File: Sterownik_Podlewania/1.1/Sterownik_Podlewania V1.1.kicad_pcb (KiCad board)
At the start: 2 copper layers, 175 x 115 mm, 76 parts, among them J1 Barrel_Jack_MountingPin, J10 Screw_Terminal_01x02, J11 Screw_Terminal_01x02, J12 Screw_Terminal_01x02, J13 Screw_Terminal_01x02, J14 Screw_Terminal_01x02, J15 Screw_Terminal_01x02, J3 RJ45, J4 Conn_01x04_Socket, J5 RJ45, J8 RJ45, J9 Screw_Terminal_01x02, SW1 SW_Nidec_CAS-120A1, SW2 SW_Nidec_CAS-120A1, SW3 SW_Push_Dual_x2, SW4 SW_Push_Dual_x2, SW5 SW_Push_Dual_x2, SW6 SW_Push_Dual_x2, U1 ESP32-DEVKITC, U10 HHG1D-1, U11 757, U2 HHG1D-1, U3 L7805, U4 LD1117S33TR_SOT223, U5 757, U7 HHG1D-1, U8 HHG1D-1, U9 HHG1D-1

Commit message: Pociągnięcie prawie wszystkich ścieżek, dodanie rezystorów do I2C 5V
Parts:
- added R12: 4k7, Resistor_SMD:R_1206_3216Metric, B.Cu at (110.0, 80.0)
- added R14: 4k7, Resistor_SMD:R_1206_3216Metric, B.Cu at (106.5, 80.0)
- R21: value 130 -> 1300
- moved R10 56.6 mm to (185.0, 110.5)
- moved U5 22.3 mm to (131.7, 110.1), turned to 90 degrees
- moved R26 20.2 mm to (92.5, 132.5), turned to 0 degrees
- moved C3 20.2 mm to (92.5, 147.5)
- moved SW3 20.0 mm to (112.5, 140.6)
- moved R27 20.0 mm to (112.7, 132.5)
- moved SW4 20.0 mm to (92.5, 140.7)
- moved C4 19.9 mm to (112.5, 147.5)
- moved U11 19.4 mm to (154.3, 109.9), turned to 90 degrees
- moved J14 15.0 mm to (220.0, 70.0)
- moved J15 15.0 mm to (220.0, 55.0)
- moved R1 5.59 mm to (185.0, 86.5), turned to 90 degrees
- moved R2 2.50 mm to (185.0, 91.5)
- moved R3 2.50 mm to (211.5, 45.0)
- moved R5 2.50 mm to (211.5, 60.0)
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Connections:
- U1 pad 12: /DS_WYJŚCIE -> unconnected-(U1-IO14-Pad12)
- U1 pad 9: unconnected-(U1-IO25-Pad9) -> /DS_WYJŚCIE
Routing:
- net +5V: track 0.00 -> 342.0 mm
- net VP: track 0.00 -> 245.7 mm
- net +3.3V: track 0.00 -> 237.8 mm, vias 0 -> 1
- net SDA: track 0.00 -> 181.4 mm
- net SCL: track 0.00 -> 178.2 mm
- net Net-(J5-Pad7): track 0.00 -> 139.8 mm
- net /Pompa_230_5V: track 0.00 -> 138.9 mm, vias 0 -> 1
- net /SW1: track 0.00 -> 133.8 mm
- net /SEN0193_WYJŚCIE: track 0.00 -> 133.1 mm
- net /SW2: track 0.00 -> 112.9 mm
- net /Sekcja 5_5V: track 0.00 -> 105.1 mm, vias 0 -> 2
- net /DS_WYJŚCIE: track 0.00 -> 96.0 mm
- net /SW3: track 0.00 -> 95.0 mm
- net GND_VP: track 0.00 -> 91.9 mm
- net SDA_5V: track 0.00 -> 88.8 mm
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- added copper zone on B.Cu, net +3.3V
- added copper zone on B.Cu, net GND
- added copper zone on F.Cu, net GND

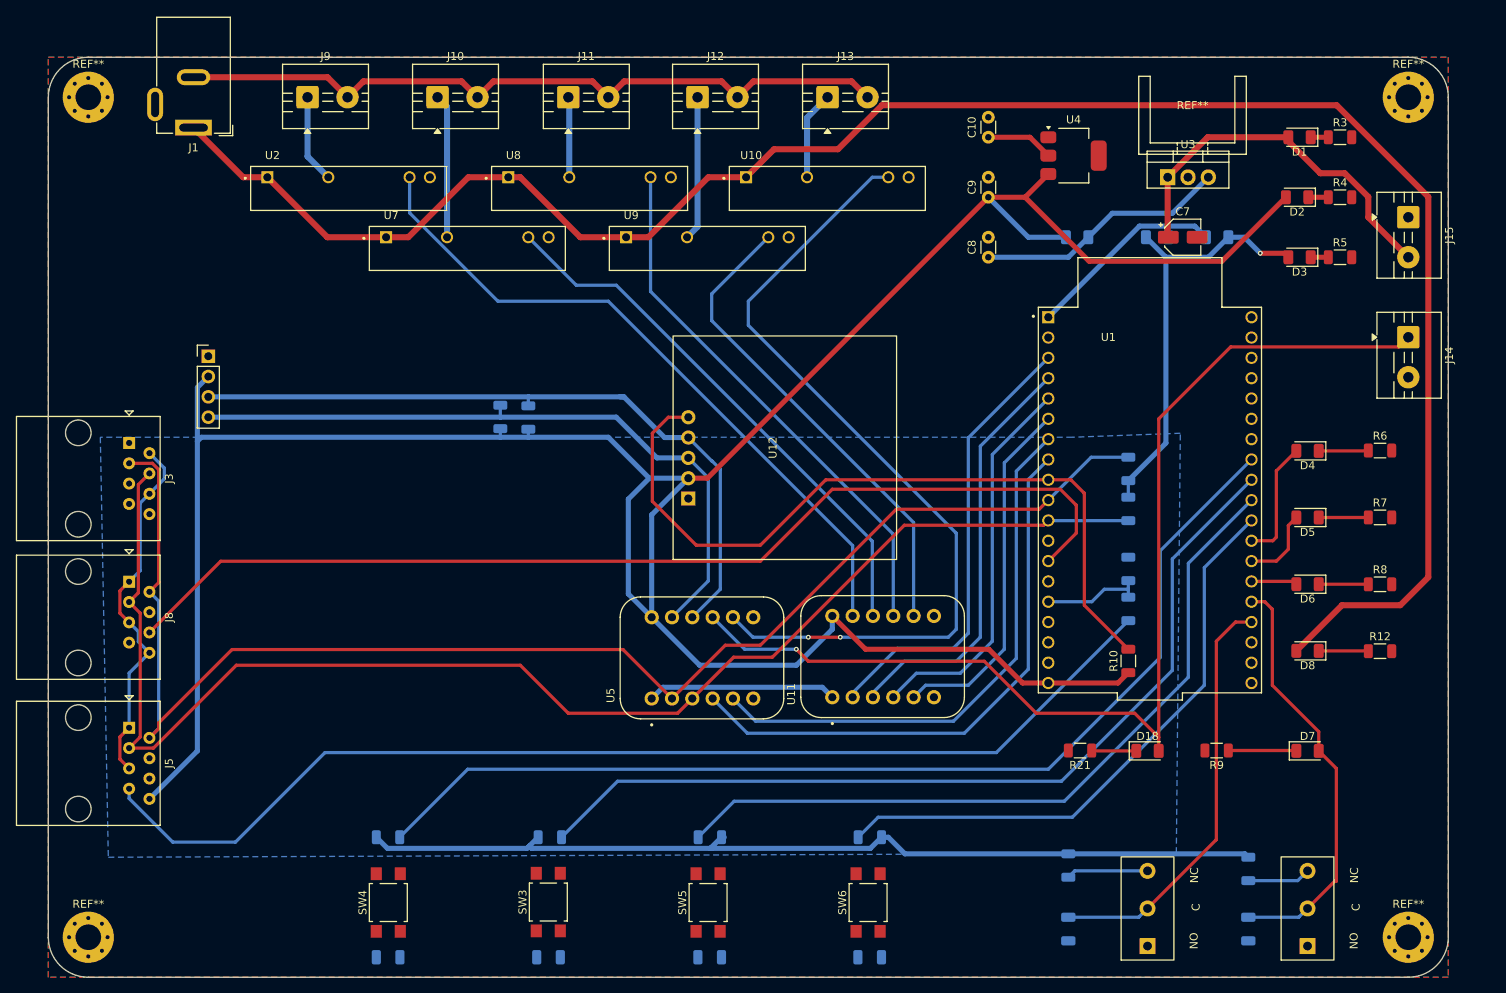
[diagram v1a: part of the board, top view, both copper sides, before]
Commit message: Poprawiono błędy połączeń SDA,SCL, dodno drugą magistralę I2C, pociągnięcie nowych ścieżek
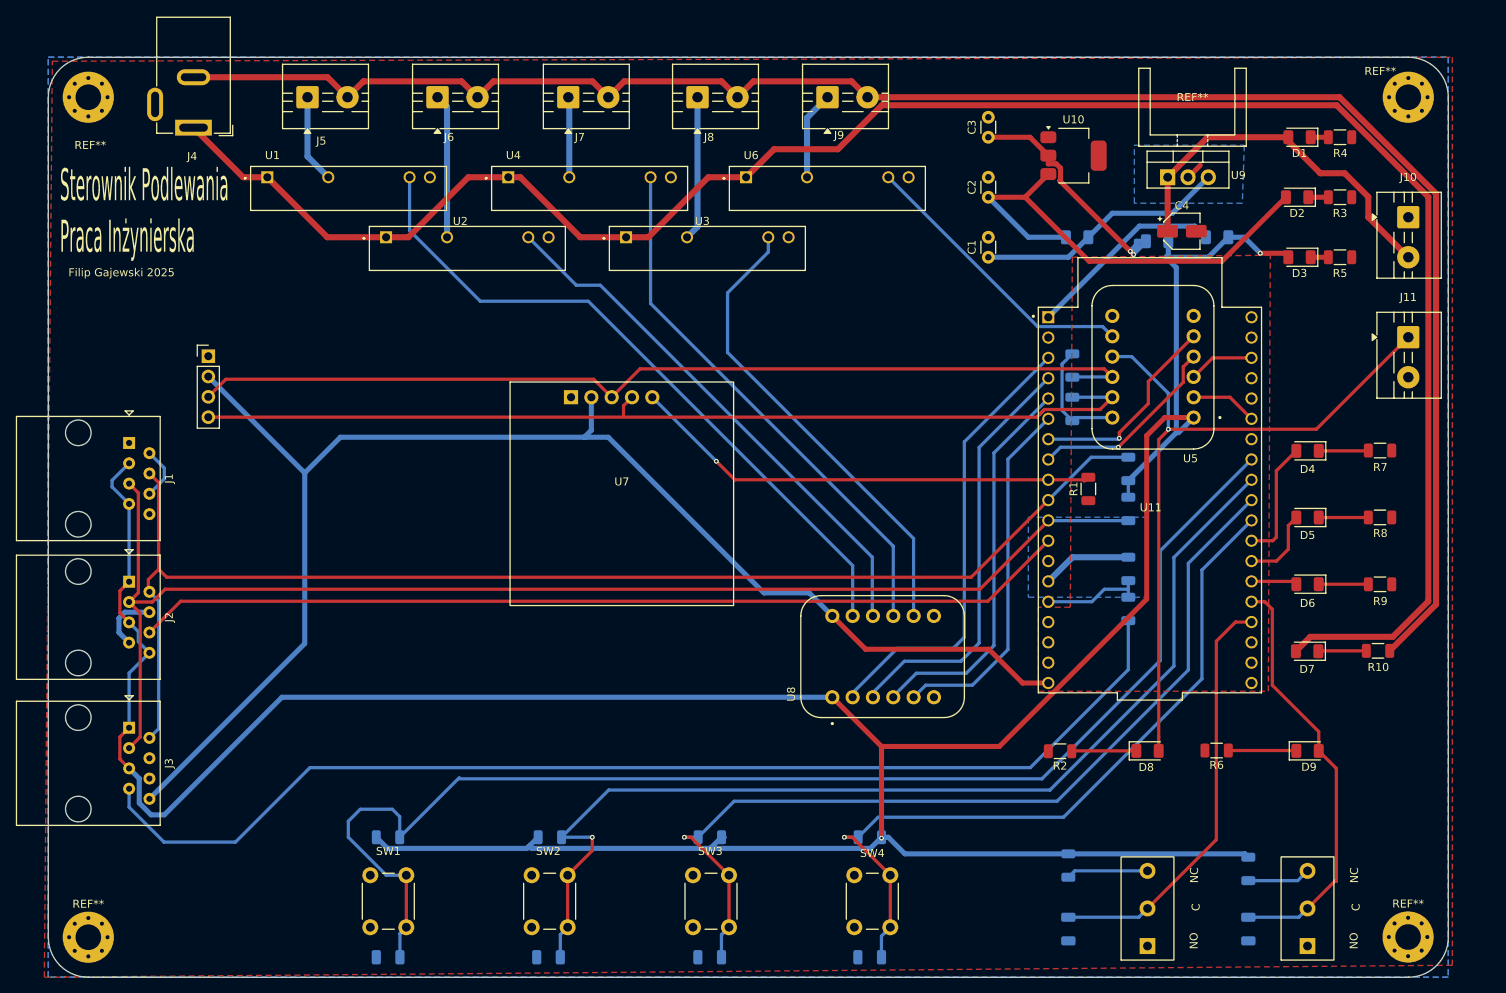
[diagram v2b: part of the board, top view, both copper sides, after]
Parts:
- removed the D8 at (207.4, 109.2)
- removed the R12 at (216.5, 109.2)
- removed the R21 at (179.0, 121.7)
- removed U12: ~, RTC:RTC DS1307 + 32kb EEPROM 24C32 I2C
- added D7: LED, LED_SMD:LED_1206_3216Metric, F.Cu at (207.3, 109.2)
- added R10: 2k2, Resistor_SMD:R_1206_3216Metric, F.Cu at (216.2, 109.2)
- added R2: 1300, Resistor_SMD:R_1206_3216Metric, F.Cu at (176.5, 121.8)
- added U7: ~, RTC:RTC DS1307 + 32kb EEPROM 24C32 I2C, F.Cu at (121.7, 89.6)
- SW1: renamed from SW4; footprint Button_Switch_SMD:SW_SPST_TL3305A -> Button_Switch_THT:SW_PUSH_6mm
- SW2: renamed from SW3; footprint Button_Switch_SMD:SW_SPST_TL3305A -> Button_Switch_THT:SW_PUSH_6mm
- SW3: renamed from SW5; footprint Button_Switch_SMD:SW_SPST_TL3305A -> Button_Switch_THT:SW_PUSH_6mm
- SW4: renamed from SW6; footprint Button_Switch_SMD:SW_SPST_TL3305A -> Button_Switch_THT:SW_PUSH_6mm
- moved R20 71.5 mm to (178.0, 79.0)
- moved R19 68.3 mm to (178.0, 73.5), turned to -90 degrees
- moved U5 67.1 mm to (188.1, 73.8), turned to 180 degrees
- moved R1 22.1 mm to (180.0, 89.0)
- moved SW1 3.82 mm to (90.2, 143.8)
- moved SW2 3.78 mm to (110.4, 143.8)
- moved SW3 3.62 mm to (130.6, 143.8)
- moved SW4 3.53 mm to (150.8, 143.8)
- moved REF** 1.01 mm to (193.0, 46.0)
- moved C4 0.76 mm to (191.7, 56.8)
- moved D11 0.50 mm to (188.6, 58.0), turned to 180 degrees
- renumbered C8 to C1, C3 to C10, C9 to C2, C10 to C3, C7 to C4, C1 to C5, C2 to C6, C6 to C7, C5 to C8, C4 to C9, D21 to D10, D20 to D11, D19 to D12, D18 to D8, D7 to D9, J3 to J1, J15 to J10, J14 to J11, J4 to J12, J8 to J2, J5 to J3, J1 to J4, J9 to J5, J10 to J6, J11 to J7, J12 to J8, J13 to J9, R10 to R1, R22 to R11, R1 to R12, R11 to R13, R13 to R14, R2 to R15, R23 to R16, R31 to R17, R28 to R18, R12 to R19, R14 to R20, R27 to R21, R26 to R22, R4 to R3, R3 to R4, R9 to R6, R6 to R7, R7 to R8, R8 to R9, SW2 to SW5, SW1 to SW6, U2 to U1, U4 to U10, U1 to U11, U7 to U2, U9 to U3, U8 to U4, U10 to U6, U11 to U8, U3 to U9
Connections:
- net SCL_5V renamed SCL_2_5V
- net SDA_5V renamed SDA_2_5V
- J1 pad 1: GND -> unconnected-(J1-Pad1)
- J1 pad 2: +3.3V -> GND
- J1 pad 3: SDA -> +3.3V
- J1 pad 4: SCL -> SDA_1
- J1 pad 5: GND -> SCL_1
- J1 pad 6: +3.3V -> GND
- J1 pad 7: unconnected-(J3-Pad7) -> +3.3V
- J2 pad 2: SDA -> SDA_1
- J2 pad 3: SCL -> SCL_1
- J3 pad 2: SDA -> SDA_1
- J3 pad 3: SCL -> SCL_1
- R12 pad 2: SDA -> SDA_1
- R15 pad 2: SCL -> SCL_1
- U11 pad 10: SDA -> SDA_1
- U11 pad 11: SCL -> SCL_1
- U11 pad 12: unconnected-(U1-IO14-Pad12) -> /SEN0193_WYJŚCIE
- U11 pad 13: /SEN0193_WYJŚCIE -> unconnected-(U11-IO12-Pad13)
- U11 pad 33: unconnected-(U1-IO21-Pad33) -> SCL_2
- U11 pad 36: unconnected-(U1-IO22-Pad36) -> SDA_2
- U5 pad A1: SDA -> SCL_2
- U5 pad A2: SCL -> SDA_2
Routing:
- net SDA: track 181.4 -> 0.00 mm
- net SCL: track 178.2 -> 0.00 mm
- net SCL_1: track 0.00 -> 164.3 mm
- net +3.3V: track 237.8 -> 401.0 mm, vias 1 -> 2
- net SDA_1: track 0.00 -> 162.9 mm
- net GND_VP: track 91.9 -> 227.5 mm
- net +5V: track 342.0 -> 253.3 mm
- net /Sekcja 5_5V: track 105.1 -> 36.2 mm, vias 2 -> 0
- net /Pompa_230_5V: track 138.9 -> 88.8 mm
- net /Pompa_230: track 71.8 -> 24.6 mm, vias 0 -> 1
- net /Sekcja 5: track 68.9 -> 25.7 mm, vias 0 -> 1
- net SCL_2_5V: track 86.5 -> 122.8 mm
- net /DS_WYJŚCIE: track 96.0 -> 59.8 mm, vias 0 -> 1
- net SDA_2_5V: track 88.8 -> 121.8 mm
- net /SW1: track 133.8 -> 165.9 mm
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- added copper zone on F.Cu, net +5V
- removed copper zone on B.Cu, net +3.3V
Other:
- board text added: "Filip Gajewski 2025"
- board text added: "Sterownik Podlewania Praca Inżynierska"

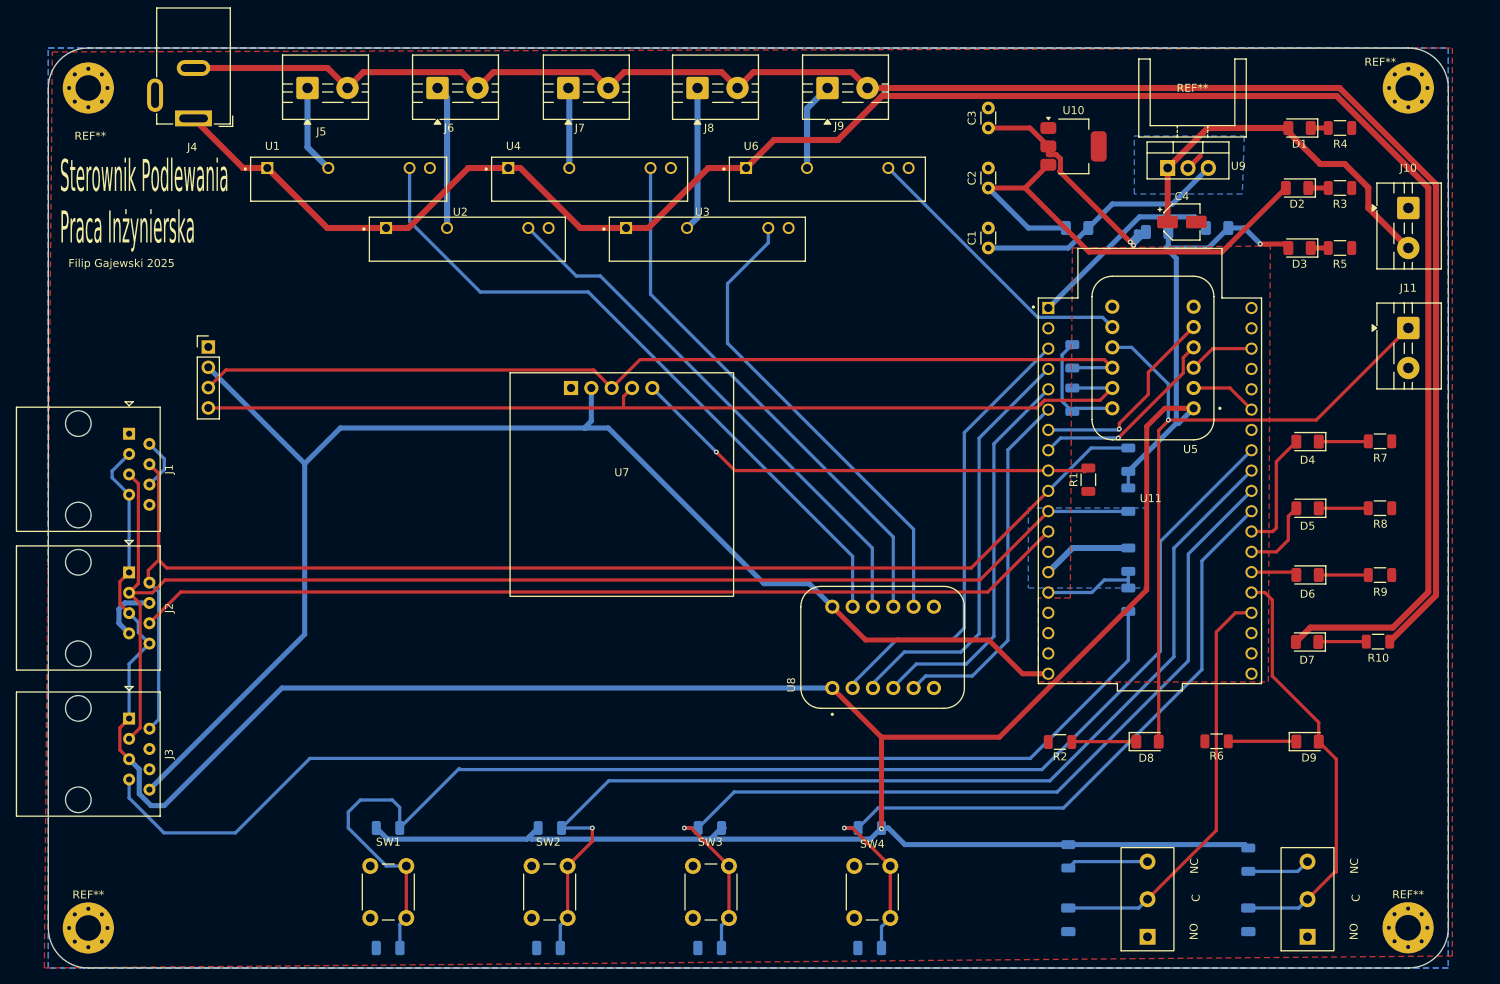
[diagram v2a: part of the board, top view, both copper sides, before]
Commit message: Usunięcie zewnętrzego zasilania 12 i stabilizatora napięcia, korekcja zasilania wzmacniacz operacyjny moduł zasilania
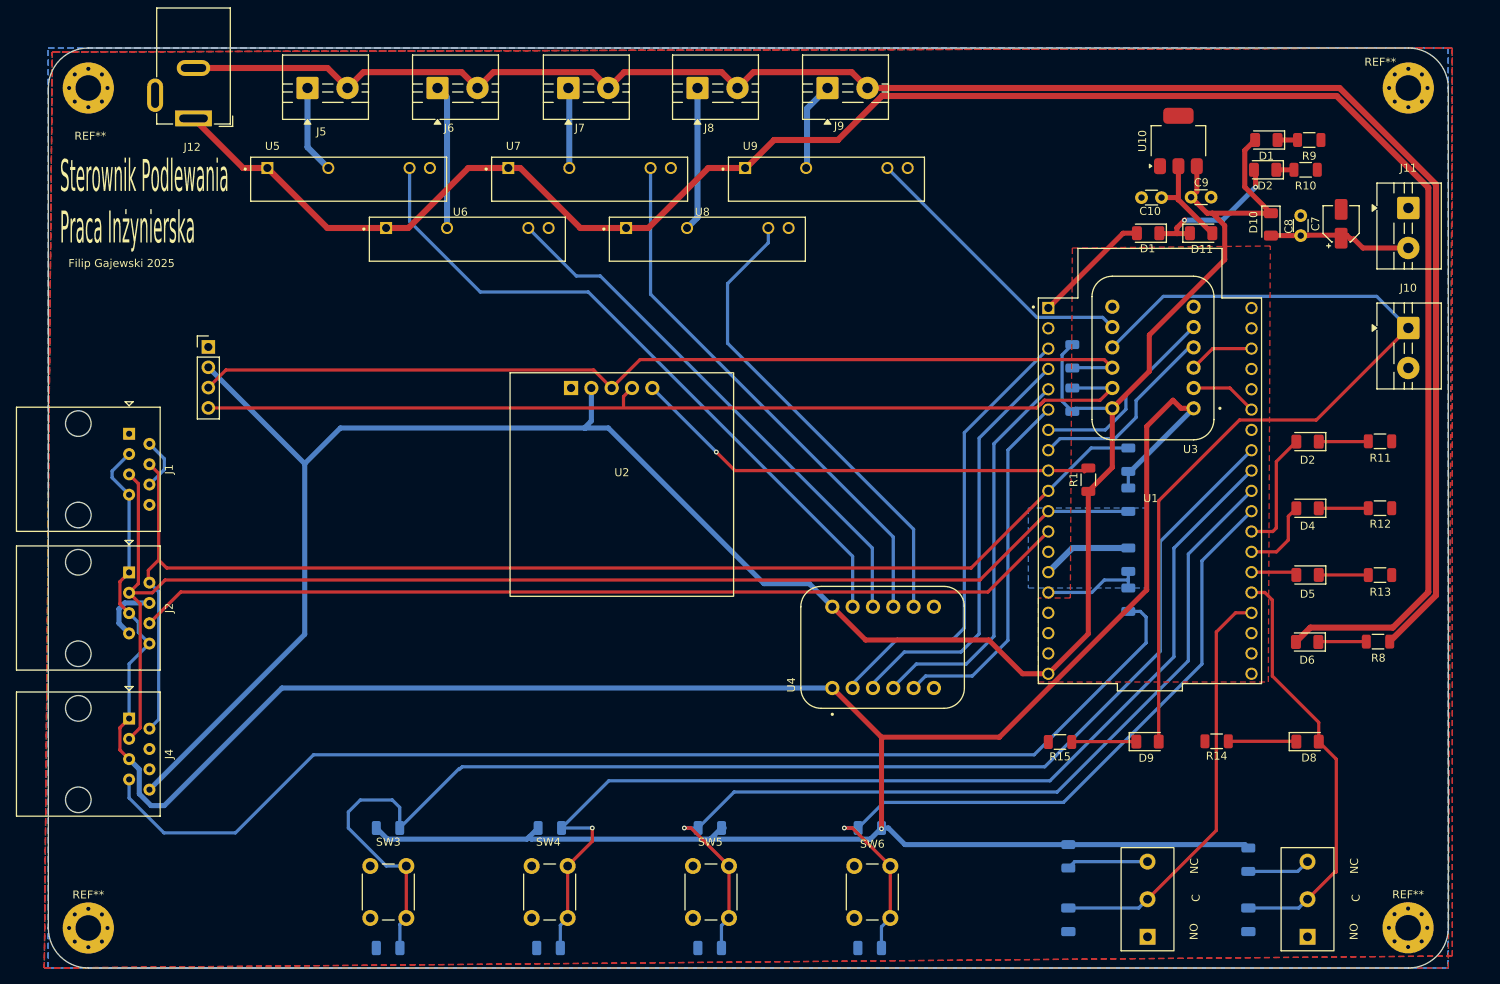
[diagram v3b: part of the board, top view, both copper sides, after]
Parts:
- removed the C1 at (167.5, 60.0)
- removed the C2 at (167.5, 52.5)
- removed the C4 at (191.7, 56.8)
- removed the D1 at (206.4, 45.0)
- removed D12: D_Schottky, Diode_SMD:D_1206_3216Metric
- removed the R4 at (211.5, 45.0)
- removed the REF** at (193.0, 46.0)
- removed the U9 at (189.9, 50.0)
- added C7: 0.33u, Capacitor_SMD:CP_Elec_4x5.4, F.Cu at (211.6, 57.0)
- added C8: 0.1u, Capacitor_THT:C_Disc_D3.0mm_W1.6mm_P2.50mm, F.Cu at (206.6, 58.5)
- added C9: 0.1u, Capacitor_THT:C_Disc_D3.0mm_W1.6mm_P2.50mm, F.Cu at (192.8, 53.6)
- added D10: D_Schottky, Diode_SMD:D_1206_3216Metric, F.Cu at (202.8, 57.0)
- D1: renamed from D10; moved to F.Cu
- D11: moved to F.Cu
- moved C10 23.3 mm to (189.2, 53.7), turned to 180 degrees
- moved U10 13.1 mm to (191.3, 46.6), turned to 90 degrees
- moved D2 10.7 mm to (202.1, 50.2)
- moved R10 10.7 mm to (207.2, 50.2)
- moved D1 8.65 mm to (187.5, 58.1)
- moved D1 7.13 mm to (202.2, 46.5)
- moved R9 7.13 mm to (207.6, 46.5)
- moved D11 5.50 mm to (194.1, 58.1), turned to 0 degrees
- moved U9 0.12 mm to (147.3, 51.4)
- renumbered C5 to C1, C3 to C10, C6 to C2, C10 to C3, C9 to C4, C8 to C5, C7 to C6, D2 to D1, D3 to D2, D4 to D2, D5 to D4, D6 to D5, D7 to D6, D9 to D8, D8 to D9, J11 to J10, J10 to J11, J4 to J12, J12 to J3, J3 to J4, R5 to R10, R7 to R11, R8 to R12, R9 to R13, R6 to R14, R2 to R15, R11 to R16, R16 to R17, R22 to R18, R21 to R19, R13 to R2, R18 to R20, R17 to R21, R14 to R3, R12 to R4, R15 to R5, R19 to R6, R20 to R7, R10 to R8, R3 to R9, SW6 to SW1, SW5 to SW2, SW1 to SW3, SW2 to SW4, SW3 to SW5, SW4 to SW6, U11 to U1, U7 to U2, U5 to U3, U8 to U4, U1 to U5, U2 to U6, U4 to U7, U3 to U8, U6 to U9
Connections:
- J11 pad 2: VSS -> Net-(D10-A)
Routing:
- net VSS: track 46.9 -> 0.00 mm
- net +5V: track 253.3 -> 287.0 mm
- net Net-(D12-A): track 31.6 -> 0.00 mm
- net /Pompa_230_5V: track 88.8 -> 111.5 mm, vias 1 -> 0
- net +3.3V: track 401.0 -> 378.8 mm, vias 2 -> 3
- net Net-(D11-A): track 30.9 -> 12.4 mm, vias 2 -> 0
- net Net-(D10-A): track 0.00 -> 17.9 mm
- net Net-(D1-A): track 25.0 -> 14.9 mm
- net Net-(J4-Pad7): track 144.1 -> 146.8 mm
- net Net-(D1-K): track 2.20 -> 0.00 mm
- net GND: track 27.8 -> 25.6 mm
- net /Sekcja 5: track 25.7 -> 24.6 mm, vias 1 -> 0
- net /Pompa_230: track 24.6 -> 24.8 mm, vias 1 -> 0
